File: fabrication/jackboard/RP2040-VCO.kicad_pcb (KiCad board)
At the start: 2 copper layers, 20 x 110 mm, 11 parts, among them J1 V/oct, J3 Inv CV, J4 Conn_01x06_Female, J5 Conn_01x08_Female, J8 Out, SW1 SW_SPDT, SW2 SW_MEC_LOW_PROF_LED

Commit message: update to v1.1
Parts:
- added H3: SpacerHoles, MountingHole:MountingHole_3.2mm_M3, F.Cu at (90.5, 96.0)
- moved J6 16.5 mm to (92.2, 49.5)
- renumbered J8 to J3, J1 to J4, J3 to J5, J4 to J6, J5 to J7, R9 to R16
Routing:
- net +3V3: track 34.4 -> 27.0 mm
- net /InvPot: track 45.5 -> 43.4 mm
- net +5V: track 38.8 -> 37.1 mm
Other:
- board text added: "RP2040 VCO V1.1 BleepSound 2023"
- board text removed: "RP2040 VCO V1.0 BleepSound 2023"

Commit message: update board with pullup on switch
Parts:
- added R17: 10k, Resistor_SMD:R_0805_2012Metric_Pad1.20x1.40mm_HandSolder, F.Cu at (87.9, 118.0)
- moved R7 2.18 mm to (87.9, 120.1), turned to 180 degrees
- renumbered H3 to H2, J3 to J1, J6 to J2, J7 to J4, J4 to J6, J5 to J7, R16 to R7, SW2 to SW1, SW1 to SW2
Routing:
- net +3V3: track 27.0 -> 79.9 mm, vias 0 -> 1
- net /Push_SW: track 59.2 -> 65.3 mm
- net +12V: track 47.5 -> 43.6 mm
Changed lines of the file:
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@@
     (property "ki_keywords" "audio jack receptacle mono headphones phone TS connector")
     (attr through_hole)
-    (fp_text reference "J5" (at -4.03 1.08 180) (layer "F.SilkS")
+    (fp_text reference "J7" (at -4.03 1.08 180) (layer "F.SilkS")
         (effects (font (size 1 1) (thickness 0.15)))
     )
@@
     (property "ki_keywords" "audio jack receptacle mono headphones phone TS connector")
     (attr through_hole)
-    (fp_text reference "J4" (at -4.03 1.08 180) (layer "F.SilkS")
+    (fp_text reference "J6" (at -4.03 1.08 180) (layer "F.SilkS")
         (effects (font (size 1 1) (thickness 0.15)))
     )
@@
     (property "ki_keywords" "audio jack receptacle mono headphones phone TS connector")
     (attr through_hole)
-    (fp_text reference "J3" (at -4.03 1.08 180) (layer "F.SilkS")
+    (fp_text reference "J1" (at -4.03 1.08 180) (layer "F.SilkS")
         (effects (font (size 1 1) (thickness 0.15)))
     )
@@
     (property "ki_keywords" "switch normally-open pushbutton push-button LED")
     (attr through_hole)
-    (fp_text reference "SW2" (at 0 5 unlocked) (layer "F.SilkS")
+    (fp_text reference "SW1" (at 0 5 unlocked) (layer "F.SilkS")
         (effects (font (size 1 1) (thickness 0.15)))
     )
@@
     (property "Sheetfile" "RP2040-VCO.kicad_sch")
     (property "Sheetname" "")
+    (property "exclude_from_bom" "")
     (property "ki_description" "Mounting Hole without connection")
     (property "ki_keywords" "mounting hole")
-    (attr exclude_from_pos_files)
-    (fp_text reference "H3" (at -4.5 0) (layer "F.SilkS")
+    (attr exclude_from_pos_files exclude_from_bom)
+    (fp_text reference "H2" (at -4.5 0) (layer "F.SilkS")
         (effects (font (size 1 1) (thickness 0.15)))
     )
@@
   )
   (footprint "Resistor_SMD:R_0805_2012Metric_Pad1.20x1.40mm_HandSolder" (layer "F.Cu")
-    (at 90 119.5)
+    (at 87.9 120.1 180)
     (descr "Resistor SMD 0805 (2012 Metric), square (rectangular) end terminal, IPC_7351 nominal with elongated pad for handsoldering. (Body size source: IPC-SM-782 page 72, https://www.pcb-3d.com/wordpress/wp-content/uploads/ipc-sm-782a_amendment_1_and_2.pdf), generated with kicad-footprint-generator")
     (tags "resistor handsolder")
@@
     (property "ki_keywords" "R res resistor")
     (attr smd)
-    (fp_text reference "R16" (at 0 -1.65) (layer "F.SilkS")
+    (fp_text reference "R7" (at 2.8 0) (layer "F.SilkS")
         (effects (font (size 1 1) (thickness 0.15)))
     )
@@
     (fp_line (start 1 0.625) (end -1 0.625)
       (stroke (width 0.1) (type solid)) (layer "F.Fab"))
-    (pad "1" smd roundrect (at -1 0) (size 1.2 1.4) (layers "F.Cu" "F.Paste" "F.Mask") (roundrect_rratio 0.208333)
+    (pad "1" smd roundrect (at -1 0 180) (size 1.2 1.4) (layers "F.Cu" "F.Paste" "F.Mask") (roundrect_rratio 0.208333)
       (net 17 "Net-(R7-Pad1)") (pintype "passive"))
-    (pad "2" smd roundrect (at 1 0) (size 1.2 1.4) (layers "F.Cu" "F.Paste" "F.Mask") (roundrect_rratio 0.208333)
+    (pad "2" smd roundrect (at 1 0 180) (size 1.2 1.4) (layers "F.Cu" "F.Paste" "F.Mask") (roundrect_rratio 0.208333)
       (net 2 "+12V") (pintype "passive"))
+    (model "${KICAD6_3DMODEL_DIR}/Resistor_SMD.3dshapes/R_0805_2012Metric.wrl"
+      (offset (xyz 0 0 0))
+      (scale (xyz 1 1 1))
+      (rotate (xyz 0 0 0))
+    )
+  )
+  (footprint "Resistor_SMD:R_0805_2012Metric_Pad1.20x1.40mm_HandSolder" (layer "F.Cu")
+    (at 87.9 118 180)
+    (descr "Resistor SMD 0805 (2012 Metric), square (rectangular) end terminal, IPC_7351 nominal with elongated pad for handsoldering. (Body size source: IPC-SM-782 page 72, https://www.pcb-3d.com/wordpress/wp-content/uploads/ipc-sm-782a_amendment_1_and_2.pdf), generated with kicad-footprint-generator")
+    (tags "resistor handsolder")
+    (property "Comment " "1/4W, 1%")
+    (property "MFN" "YAGEO")
+    (property "MFP" "RC0805FR-1010KL")
+    (property "Sheetfile" "RP2040-VCO.kicad_sch")
+    (property "Sheetname" "")
+    (property "ki_description" "Resistor")
+    (property "ki_keywords" "R res resistor")
+    (attr smd)
+    (fp_text reference "R17" (at 3.3 0) (layer "F.SilkS")
+        (effects (font (size 1 1) (thickness 0.15)))
+    )
+    (fp_text value "10k" (at 0 1.65) (layer "F.Fab")
+        (effects (font (size 1 1) (thickness 0.15)))
+    )
+    (fp_text user "${REFERENCE}" (at 0 0) (layer "F.Fab")
+        (effects (font (size 0.5 0.5) (thickness 0.08)))
+    )
+    (fp_line (start -0.227064 -0.735) (end 0.227064 -0.735)
+      (stroke (width 0.12) (type solid)) (layer "F.SilkS"))
+    (fp_line (start -0.227064 0.735) (end 0.227064 0.735)
+      (stroke (width 0.12) (type solid)) (layer "F.SilkS"))
+    (fp_line (start -1.85 -0.95) (end 1.85 -0.95)
+      (stroke (width 0.05) (type solid)) (layer "F.CrtYd"))
+    (fp_line (start -1.85 0.95) (end -1.85 -0.95)
+      (stroke (width 0.05) (type solid)) (layer "F.CrtYd"))
+    (fp_line (start 1.85 -0.95) (end 1.85 0.95)
+      (stroke (width 0.05) (type solid)) (layer "F.CrtYd"))
+    (fp_line (start 1.85 0.95) (end -1.85 0.95)
+      (stroke (width 0.05) (type solid)) (layer "F.CrtYd"))
+    (fp_line (start -1 -0.625) (end 1 -0.625)
+      (stroke (width 0.1) (type solid)) (layer "F.Fab"))
+    (fp_line (start -1 0.625) (end -1 -0.625)
+      (stroke (width 0.1) (type solid)) (layer "F.Fab"))
+    (fp_line (start 1 -0.625) (end 1 0.625)
+      (stroke (width 0.1) (type solid)) (layer "F.Fab"))
+    (fp_line (start 1 0.625) (end -1 0.625)
+      (stroke (width 0.1) (type solid)) (layer "F.Fab"))
+    (pad "1" smd roundrect (at -1 0 180) (size 1.2 1.4) (layers "F.Cu" "F.Paste" "F.Mask") (roundrect_rratio 0.208333)
+      (net 12 "/Push_SW") (pintype "passive"))
+    (pad "2" smd roundrect (at 1 0 180) (size 1.2 1.4) (layers "F.Cu" "F.Paste" "F.Mask") (roundrect_rratio 0.208333)
+      (net 5 "+3V3") (pintype "passive"))
     (model "${KICAD6_3DMODEL_DIR}/Resistor_SMD.3dshapes/R_0805_2012Metric.wrl"
       (offset (xyz 0 0 0))
@@
     (property "ki_keywords" "switch single-pole double-throw spdt ON-ON")
     (attr through_hole)
-    (fp_text reference "SW1" (at 0.124031 -8.249895) (layer "F.SilkS") hide
+    (fp_text reference "SW2" (at 0.124031 -8.249895) (layer "F.SilkS") hide
         (effects (font (size 1 1) (thickness 0.15)))
     )
@@
     (property "ki_keywords" "connector")
     (attr through_hole)
-    (fp_text reference "J6" (at 0 2.77) (layer "B.SilkS")
+    (fp_text reference "J2" (at 0 2.77) (layer "B.SilkS")
         (effects (font (size 1 1) (thickness 0.15)) (justify mirror))
     )
@@
     (property "ki_keywords" "connector")
     (attr through_hole)
-    (fp_text reference "J7" (at 0 2.77) (layer "B.SilkS")
+    (fp_text reference "J4" (at 0 2.77) (layer "B.SilkS")
         (effects (font (size 1 1) (thickness 0.15)) (justify mirror))
     )
@@
   (via (at 82 66.6) (size 0.8) (drill 0.4) (layers "F.Cu" "B.Cu") (free) (net 1))
   (via (at 82 67.5) (size 0.8) (drill 0.4) (layers "F.Cu" "B.Cu") (free) (net 1))
-  (segment (start 89.3 117.8) (end 91 119.5) (width 0.3) (layer "F.Cu") (net 2))
-  (segment (start 81.5 117.8) (end 89.3 117.8) (width 0.3) (layer "F.Cu") (net 2))
+  (segment (start 86.9 120.1) (end 83.8 120.1) (width 0.3) (layer "F.Cu") (net 2))
+  (segment (start 83.8 120.1) (end 81.5 117.8) (width 0.3) (layer "F.Cu") (net 2))
   (via (at 81.5 117.8) (size 0.8) (drill 0.4) (layers "F.Cu" "B.Cu") (net 2))
   (segment (start 78.7 117.8) (end 74.5 113.6) (width 0.3) (layer "B.Cu") (net 2))
@@
   (segment (start 85.210489 89.760489) (end 86.5 91.05) (width 0.3) (layer "B.Cu") (net 4))
   (segment (start 85.210489 69.983413) (end 85.210489 62.789511) (width 0.3) (layer "B.Cu") (net 4))
+  (segment (start 92.3 112.6) (end 92.3 112.4) (width 0.3) (layer "F.Cu") (net 5))
+  (segment (start 86.9 118) (end 92.3 112.6) (width 0.3) (layer "F.Cu") (net 5))
+  (via (at 92.3 112.4) (size 0.8) (drill 0.4) (layers "F.Cu" "B.Cu") (net 5))
   (segment (start 86.5 50) (end 86.5 53.257057) (width 0.3) (layer "B.Cu") (net 5))
   (segment (start 86.5 53.257057) (end 91.642943 58.4) (width 0.3) (layer "B.Cu") (net 5))
   (segment (start 92.2 62.2) (end 92.2 64.76) (width 0.3) (layer "B.Cu") (net 5))
   (segment (start 93.5 59.1) (end 93.5 60.9) (width 0.3) (layer "B.Cu") (net 5))
+  (segment (start 92.3 112.4) (end 92.6 112.1) (width 0.3) (layer "B.Cu") (net 5))
   (segment (start 92.8 58.4) (end 93.5 59.1) (width 0.3) (layer "B.Cu") (net 5))
+  (segment (start 85.9 86) (end 85.9 71.06) (width 0.3) (layer "B.Cu") (net 5))
   (segment (start 93.5 60.9) (end 92.2 62.2) (width 0.3) (layer "B.Cu") (net 5))
   (segment (start 92.2 64.76) (end 86.46 70.5) (width 0.3) (layer "B.Cu") (net 5))
+  (segment (start 92.6 92.7) (end 85.9 86) (width 0.3) (layer "B.Cu") (net 5))
   (segment (start 91.642943 58.4) (end 92.8 58.4) (width 0.3) (layer "B.Cu") (net 5))
+  (segment (start 85.9 71.06) (end 86.46 70.5) (width 0.3) (layer "B.Cu") (net 5))
+  (segment (start 92.6 112.1) (end 92.6 92.7) (width 0.3) (layer "B.Cu") (net 5))
   (segment (start 82 85.2) (end 82 74.05) (width 0.3) (layer "F.Cu") (net 6))
   (segment (start 79 130.5) (end 77.35048 128.85048) (width 0.3) (layer "F.Cu") (net 6))
@@
   (segment (start 92.2 54.58) (end 88.58 54.58) (width 0.3) (layer "F.Cu") (net 11))
   (segment (start 88.58 54.58) (end 84 50) (width 0.3) (layer "F.Cu") (net 11))
+  (segment (start 91.54 120.64) (end 88.9 118) (width 0.3) (layer "F.Cu") (net 12))
   (segment (start 91.54 128.04) (end 91.54 122.96) (width 0.3) (layer "F.Cu") (net 12))
+  (segment (start 91.54 122.96) (end 91.54 120.64) (width 0.3) (layer "F.Cu") (net 12))
   (segment (start 82 82.8) (end 82 88.782924) (width 0.3) (layer "B.Cu") (net 12))
   (segment (start 80.250489 90.532435) (end 80.250489 106.150489) (width 0.3) (layer "B.Cu") (net 12))

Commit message: update fab files and repo organization
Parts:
- moved R17 4.15 mm to (91.9, 119.1), turned to 90 degrees
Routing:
- net +3V3: track 79.9 -> 99.2 mm
- net /Push_SW: track 65.3 -> 62.3 mm
- net +5V: track 37.1 -> 35.8 mm
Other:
- board text added: "RP2040 VCO V1.2 BleepSound 2023"
- board text removed: "RP2040 VCO V1.1 BleepSound 2023"

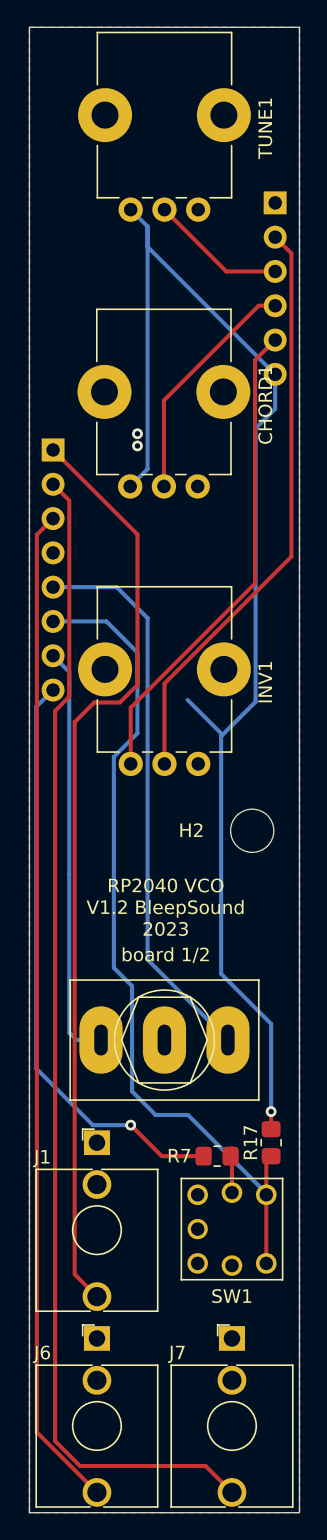
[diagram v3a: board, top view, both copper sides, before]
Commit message: fix led button footprint
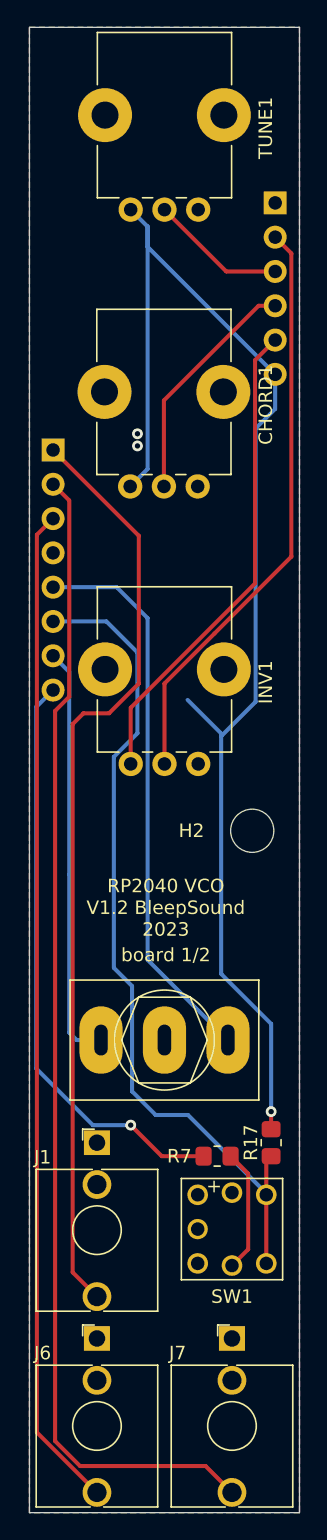
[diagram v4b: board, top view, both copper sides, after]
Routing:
- net Net-(R7-Pad1): track 3.30 -> 9.14 mm
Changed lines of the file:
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@@
         (effects (font (size 1 1) (thickness 0.15)))
+    )
+    (fp_text user "+" (at -1.9 -2.6 unlocked) (layer "F.SilkS")
+        (effects (font (size 1 1) (thickness 0.15)) (justify left bottom))
     )
     (fp_text user "${REFERENCE}" (at 0 10.16 unlocked) (layer "F.Fab")
@@
     (pad "4" thru_hole circle (at 2.54 -2.54) (size 1.524 1.524) (drill 1) (layers "*.Cu" "*.Mask")
       (net 12 "/Push_SW") (pinfunction "4") (pintype "passive"))
-    (pad "L1" thru_hole circle (at 0 -2.7) (size 1.524 1.524) (drill 1) (layers "*.Cu" "*.Mask")
+    (pad "L1" thru_hole circle (at 0 2.7) (size 1.524 1.524) (drill 1) (layers "*.Cu" "*.Mask")
       (net 17 "Net-(R7-Pad1)") (pinfunction "L1") (pintype "passive"))
-    (pad "L2" thru_hole circle (at 0 2.7) (size 1.524 1.524) (drill 1) (layers "*.Cu" "*.Mask")
+    (pad "L2" thru_hole circle (at 0 -2.7) (size 1.524 1.524) (drill 1) (layers "*.Cu" "*.Mask")
       (net 1 "GND") (pinfunction "L2") (pintype "passive"))
   )
@@
   (segment (start 82.75 51.25) (end 82.75 52.75) (width 0.3) (layer "B.Cu") (net 5))
   (segment (start 88.2 106.6) (end 91.9 110.3) (width 0.3) (layer "B.Cu") (net 5))
-  (segment (start 82 85.2) (end 82 74.05) (width 0.3) (layer "F.Cu") (net 6))
-  (segment (start 79 130.5) (end 77.35048 128.85048) (width 0.3) (layer "F.Cu") (net 6))
-  (segment (start 77.35048 128.85048) (end 77.35048 87.94952) (width 0.3) (layer "F.Cu") (net 6))
-  (segment (start 82 74.05) (end 75.75 67.8) (width 0.3) (layer "F.Cu") (net 6))
-  (segment (start 78.8 86.5) (end 80.7 86.5) (width 0.3) (layer "F.Cu") (net 6))
-  (segment (start 77.35048 87.94952) (end 78.8 86.5) (width 0.3) (layer "F.Cu") (net 6))
-  (segment (start 80.7 86.5) (end 82 85.2) (width 0.3) (layer "F.Cu") (net 6))
+  (segment (start 79.9 87.3) (end 82.1 85.1) (width 0.3) (layer "F.Cu") (net 6))
+  (segment (start 77.2 128.7) (end 77.2 88.1) (width 0.3) (layer "F.Cu") (net 6))
+  (segment (start 79 130.5) (end 77.2 128.7) (width 0.3) (layer "F.Cu") (net 6))
+  (segment (start 82.1 74.15) (end 75.75 67.8) (width 0.3) (layer "F.Cu") (net 6))
+  (segment (start 82.1 85.1) (end 82.1 74.15) (width 0.3) (layer "F.Cu") (net 6))
+  (segment (start 78 87.3) (end 79.9 87.3) (width 0.3) (layer "F.Cu") (net 6))
+  (segment (start 77.2 88.1) (end 78 87.3) (width 0.3) (layer "F.Cu") (net 6))
   (segment (start 90.967919 57.12) (end 83.96 64.127919) (width 0.3) (layer "F.Cu") (net 7))
   (segment (start 92.2 57.12) (end 90.967919 57.12) (width 0.3) (layer "F.Cu") (net 7))
@@
   (segment (start 76.949511 110.949511) (end 77.5 111.5) (width 0.3) (layer "B.Cu") (net 14))
   (segment (start 75.75 83.04) (end 76.949511 84.239511) (width 0.3) (layer "B.Cu") (net 14))
-  (segment (start 89 119.5) (end 89 122.8) (width 0.3) (layer "F.Cu") (net 17))
+  (segment (start 90.2 127) (end 89 128.2) (width 0.3) (layer "F.Cu") (net 17))
+  (segment (start 88.9 120.1) (end 90.2 121.4) (width 0.3) (layer "F.Cu") (net 17))
+  (segment (start 90.2 121.4) (end 90.2 127) (width 0.3) (layer "F.Cu") (net 17))
   (zone (net 1) (net_name "GND") (layer "F.Cu") (hatch edge 0.508)
     (connect_pads (clearance 0.508))

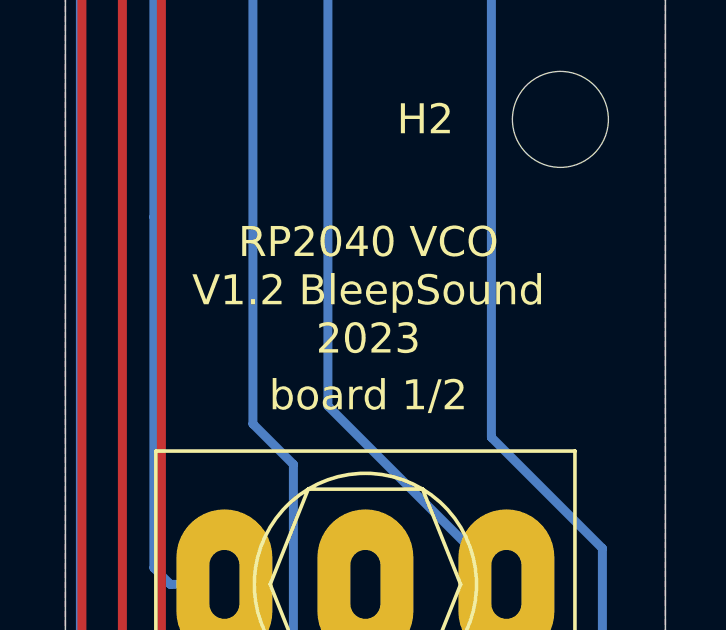
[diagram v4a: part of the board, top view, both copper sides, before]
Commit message: V1.4 update
add extra 10k resistor on inv CV input (missing)
Update BoM for clarity
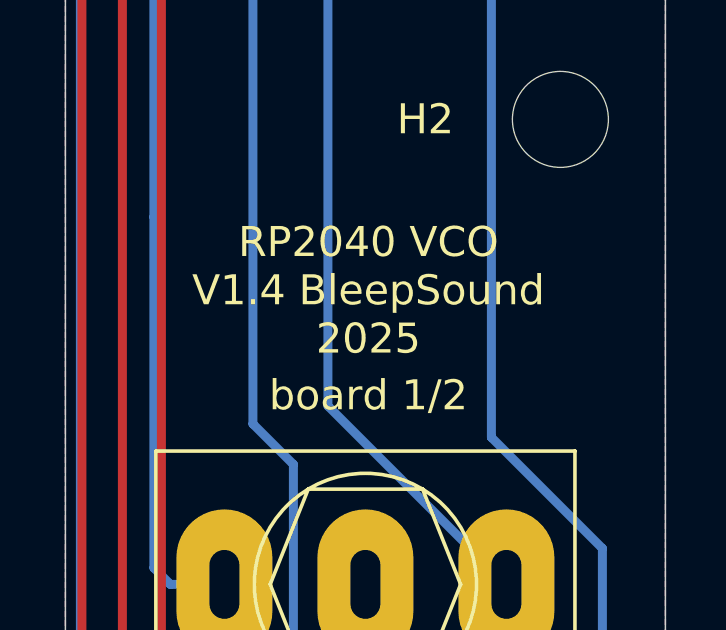
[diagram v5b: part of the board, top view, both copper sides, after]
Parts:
- R7: value 2.2k -> 330R
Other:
- board text added: "RP2040 VCO V1.4 BleepSound 2025"
- board text removed: "RP2040 VCO V1.2 BleepSound 2023"

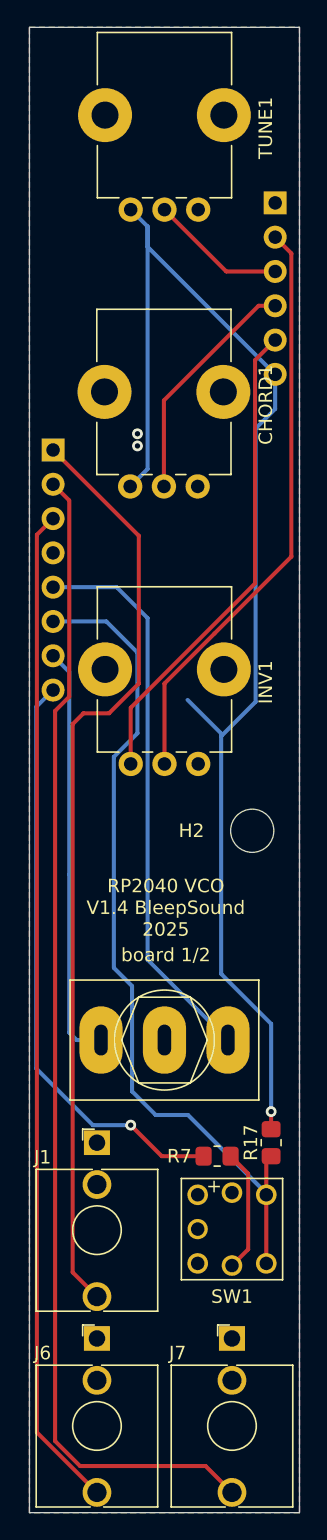
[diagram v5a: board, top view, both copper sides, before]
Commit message: v1.5
reverse pots following issue raised on github
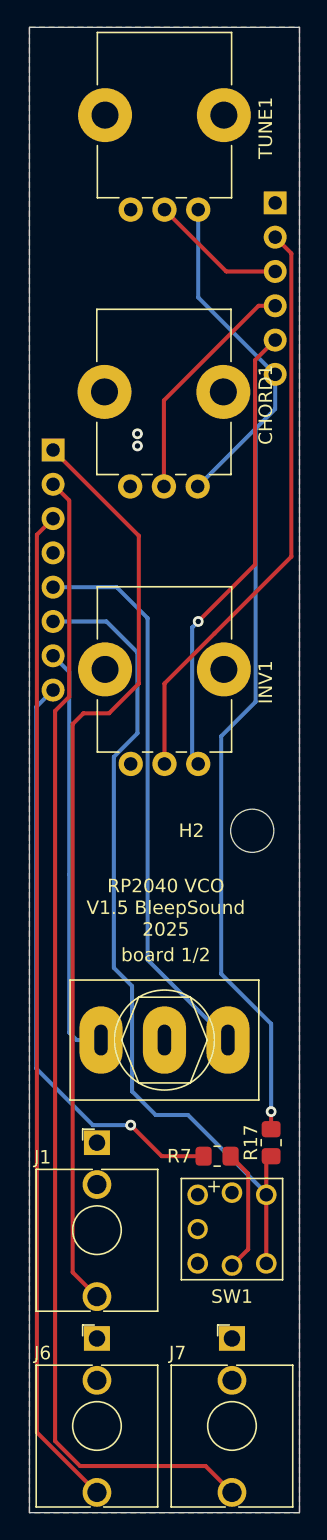
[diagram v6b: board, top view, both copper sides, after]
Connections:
- CHORD1 pad 1: +3V3 -> GND
- CHORD1 pad 3: GND -> +3V3
- INV1 pad 1: +5V -> GND
- INV1 pad 3: GND -> +5V
- TUNE1 pad 1: +3V3 -> GND
- TUNE1 pad 3: GND -> +3V3
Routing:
- net +3V3: track 99.2 -> 79.7 mm
- net +5V: track 35.8 -> 34.1 mm, vias 0 -> 1
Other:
- board text added: "RP2040 VCO V1.5 BleepSound 2025"
- board text removed: "RP2040 VCO V1.4 BleepSound 2025"
